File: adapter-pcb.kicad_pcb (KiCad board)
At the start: 2 copper layers, 90.2 x 95.9 mm, 37 parts, among them J1 SS5-80-3.50-L-D-K-TR, J2 DM3BT-DSF-PEJS, J3 Conn_02x05_Odd_Even, U1 TXS0102QDCURQ1, U2 LTC4300A-1IMS8_PBF, U3 TXS02612RTWR

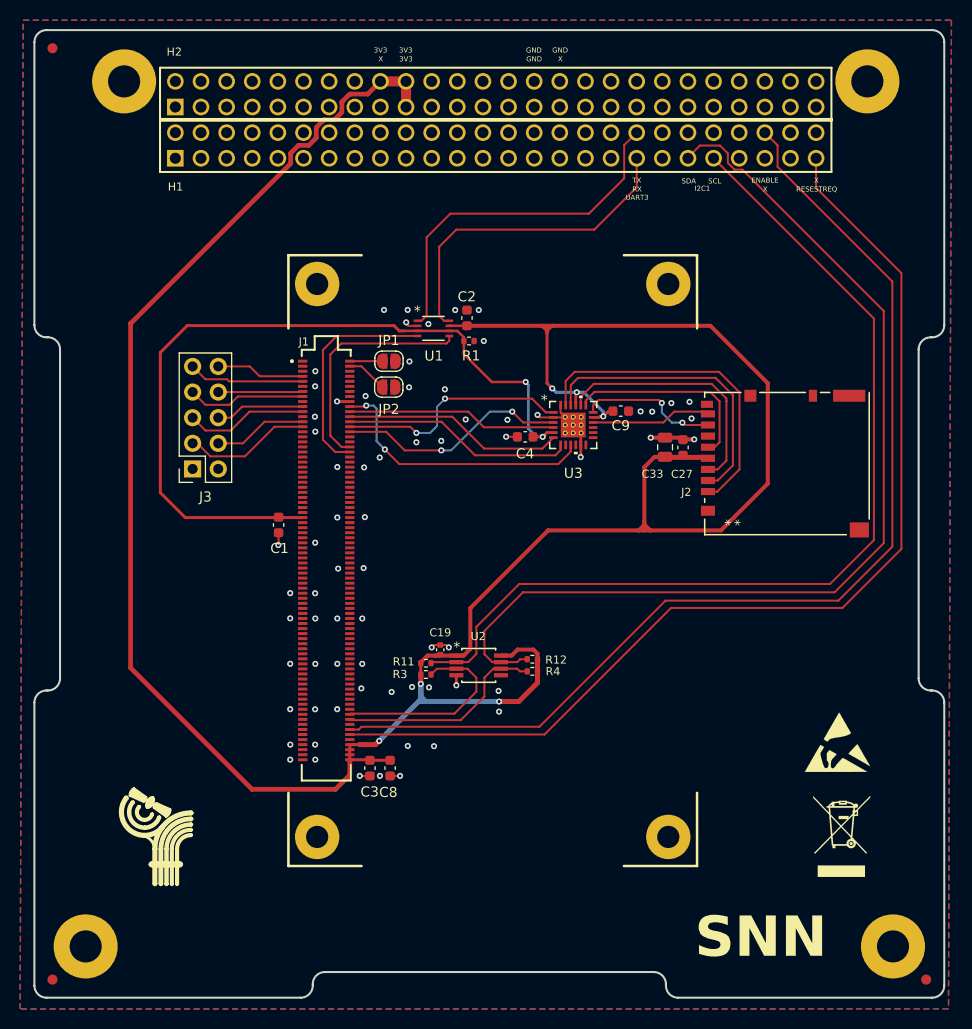
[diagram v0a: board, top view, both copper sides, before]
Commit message: Changed connector orientation and power changes
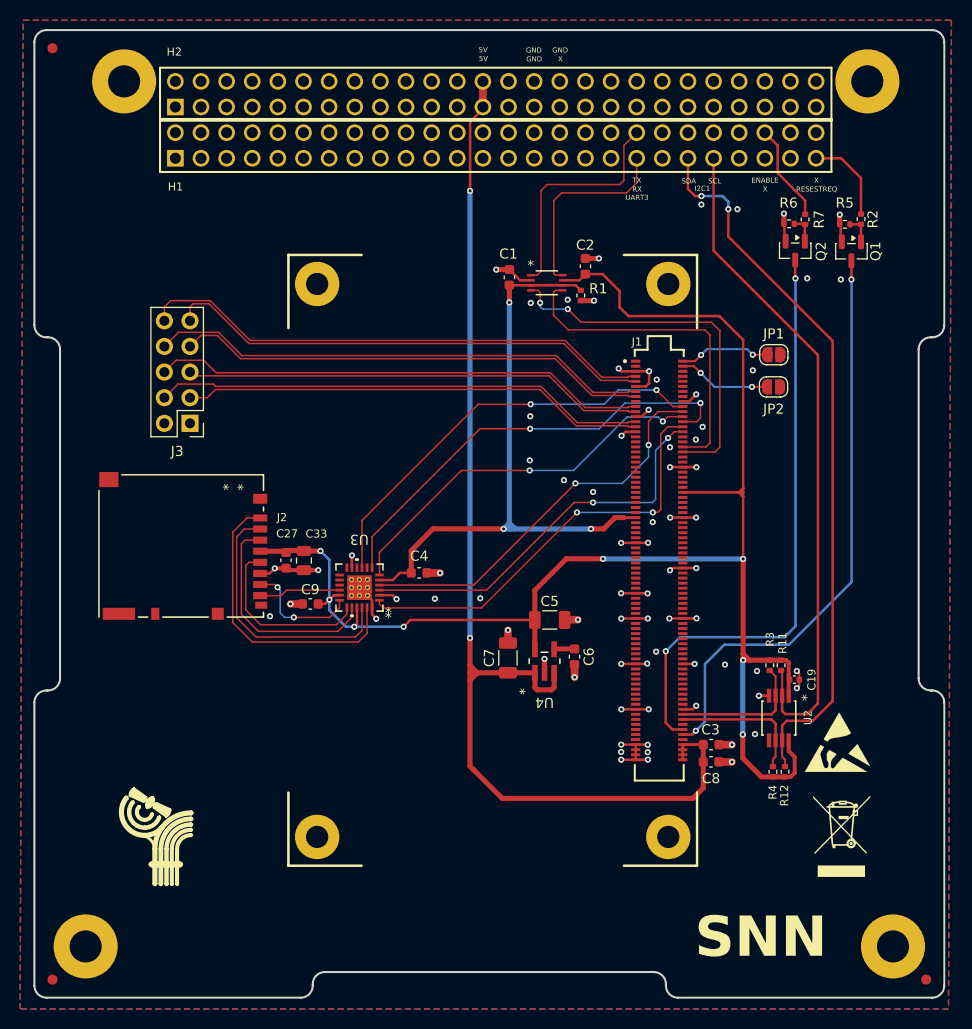
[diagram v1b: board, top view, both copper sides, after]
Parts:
- added C5: 1u, Capacitor_SMD:C_1206_3216Metric, F.Cu at (156.5, 105.0)
- added C6: 0.1u, Capacitor_SMD:C_0603_1608Metric, F.Cu at (158.9, 108.6)
- added C7: 1u, Capacitor_SMD:C_1206_3216Metric, F.Cu at (152.3, 108.7)
- added Q1: 2N7002KQ-7, Package_TO_SOT_SMD:SOT-23, F.Cu at (186.4, 68.4)
- added Q2: 2N7002KQ-7, Package_TO_SOT_SMD:SOT-23, F.Cu at (180.8, 68.4)
- added R2: 100, Resistor_SMD:R_0402_1005Metric, F.Cu at (187.3, 65.2)
- added R5: 100K, Resistor_SMD:R_0402_1005Metric, F.Cu at (185.7, 65.7)
- added R6: 100K, Resistor_SMD:R_0402_1005Metric, F.Cu at (180.2, 65.7)
- added R7: 100, Resistor_SMD:R_0402_1005Metric, F.Cu at (181.8, 65.3)
- added U4: TPS79933QDDCRQ1, adapter:DDC5, F.Cu at (156.0, 109.0)
- J3: moved to B.Cu
- moved MH5 64.9 mm to (168.2, 126.5), turned to 180 degrees
- moved MH6 64.9 mm to (133.4, 126.5), turned to 180 degrees
- moved MH7 64.9 mm to (168.2, 71.7), turned to 180 degrees
- moved MH8 64.9 mm to (133.4, 71.7), turned to 180 degrees
- moved J2 60.6 mm to (120.0, 97.6), turned to -90 degrees
- moved C27 40.9 mm to (130.3, 99.0), turned to -90 degrees
- moved JP1 38.1 mm to (178.7, 78.7)
- moved JP2 38.1 mm to (178.7, 81.9)
- moved C33 37.5 mm to (132.1, 99.1), turned to -90 degrees
- moved C9 36.2 mm to (132.8, 103.4), turned to 0 degrees
- moved C19 35.2 mm to (180.7, 110.9), turned to 180 degrees
- moved R11 35.2 mm to (179.4, 109.5), turned to -90 degrees
- moved R3 34.1 mm to (178.3, 109.5), turned to -90 degrees
- moved C3 33.9 mm to (172.5, 117.3), turned to 0 degrees
- moved C1 33.5 mm to (152.5, 71.0), turned to -90 degrees
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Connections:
- C3 pad 1: +3V3 -> +5V
- C8 pad 2: +3V3 -> +5V
- H1 pad 51: /CSKB/RESETREQ -> /CSKB/RESET
- H2 pad 18: +3V3 -> unconnected-(H2-Pin_18-Pad18)
- H2 pad 19: +3V3 -> unconnected-(H2-Pin_19-Pad19)
- H2 pad 20: +3V3 -> unconnected-(H2-Pin_20-Pad20)
- H2 pad 25: unconnected-(H2-Pin_25-Pad25) -> +5V
- H2 pad 26: unconnected-(H2-Pin_26-Pad26) -> +5V
- J1 pad 101: (no net) -> unconnected-(J1A-PF3_P-Pad101)
- J1 pad 148: /CSKB/ENABLE -> /TE0724 Connector/ONKEY
- J1 pad 150: /CSKB/RESETREQ -> /TE0724 Connector/RESETREQ
- J1 pad 154: +3V3 -> +5V
- J1 pad 156: +3V3 -> +5V
- J1 pad 158: +3V3 -> +5V
- J1 pad 160: +3V3 -> +5V
- J1 pad 34: unconnected-(J1A-SD-CD_R-Pad34) -> GND
- J1 pad 54: unconnected-(J1A-VCCIO35-Pad54) -> +3V3
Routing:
- net +5V: track 0.00 -> 114.7 mm, vias 0 -> 2
- net +3V3: track 264.4 -> 154.8 mm, vias 6 -> 8
- net /CSKB/RESETREQ: track 104.5 -> 0.00 mm
- net /CSKB/ENABLE: track 107.6 -> 9.74 mm
- net /TE0724 Connector/ONKEY: track 0.00 -> 59.3 mm, vias 0 -> 2
- net GND: track 22.1 -> 80.4 mm, vias 70 -> 75
- net /TE0724 Connector/RESETREQ: track 0.00 -> 58.2 mm, vias 0 -> 2
- net PHY_MDI0_P: track 8.80 -> 51.5 mm
- net PHY_MDI1_P: track 8.49 -> 49.8 mm
- net PHY_MDI2_P: track 8.82 -> 49.2 mm
- net PHY_MDI3_P: track 9.25 -> 48.9 mm
- net PHY_MDI0_N: track 11.5 -> 48.9 mm
- net PHY_MDI1_N: track 11.8 -> 47.1 mm
- net PHY_MDI2_N: track 12.2 -> 45.8 mm
- net PHY_MDI3_N: track 12.7 -> 46.0 mm
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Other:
- board text added: "5V"
- board text removed: "3V3"

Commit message: reviewed changes to PCB
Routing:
- net /CSKB/UART-TXD LS: track 23.4 -> 19.2 mm
- net /CSKB/UART-RXD LS: track 19.6 -> 15.4 mm
- net /SD Level Shifter/SD-D3: track 39.4 -> 36.6 mm
- net /SD Level Shifter/SD-D2: track 42.5 -> 40.2 mm
- net /SD Level Shifter/SD-CMD: track 39.3 -> 37.2 mm
- net /CSKB/I2C_SDA_CSKB: track 71.6 -> 70.1 mm
- net /TE0724 Connector/ONKEY: track 59.3 -> 57.8 mm
- net /SD Level Shifter/SD-D1: track 44.5 -> 43.5 mm

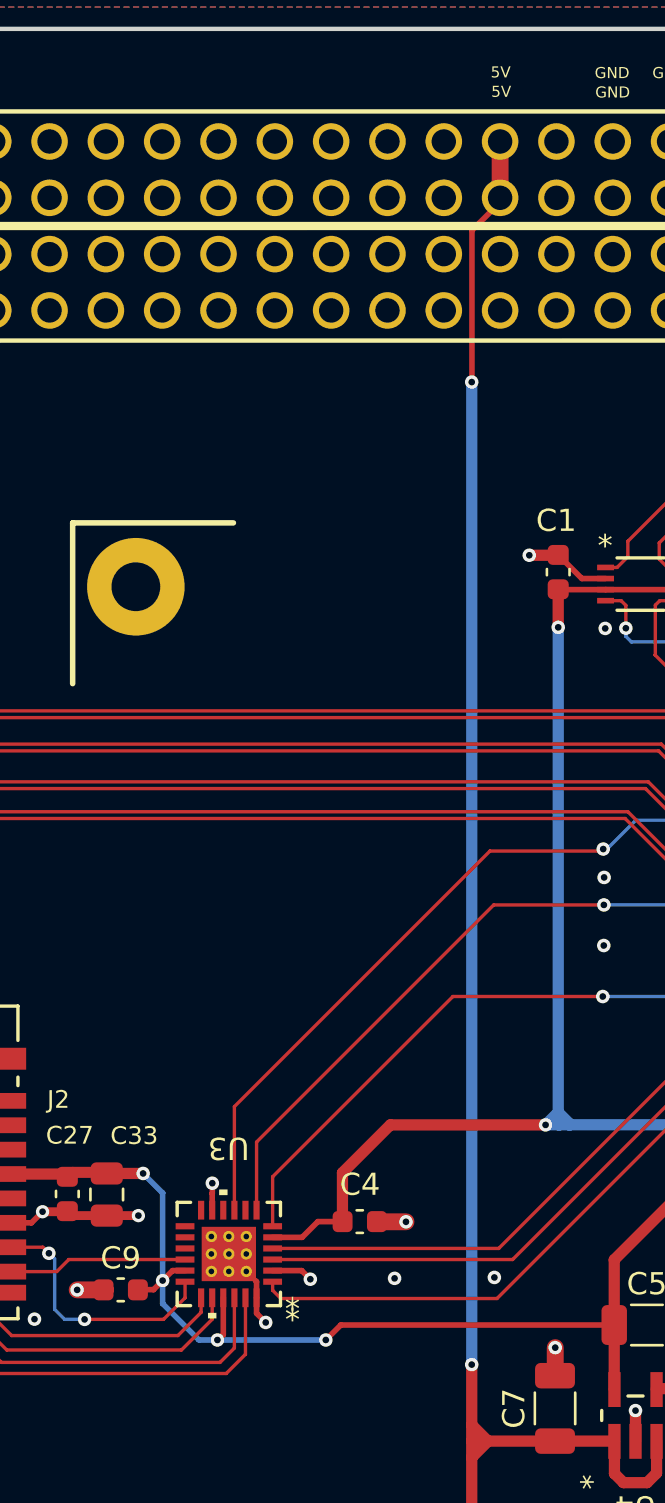
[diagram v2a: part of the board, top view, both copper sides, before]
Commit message: added mroe GND pins and moved power to PDM lines
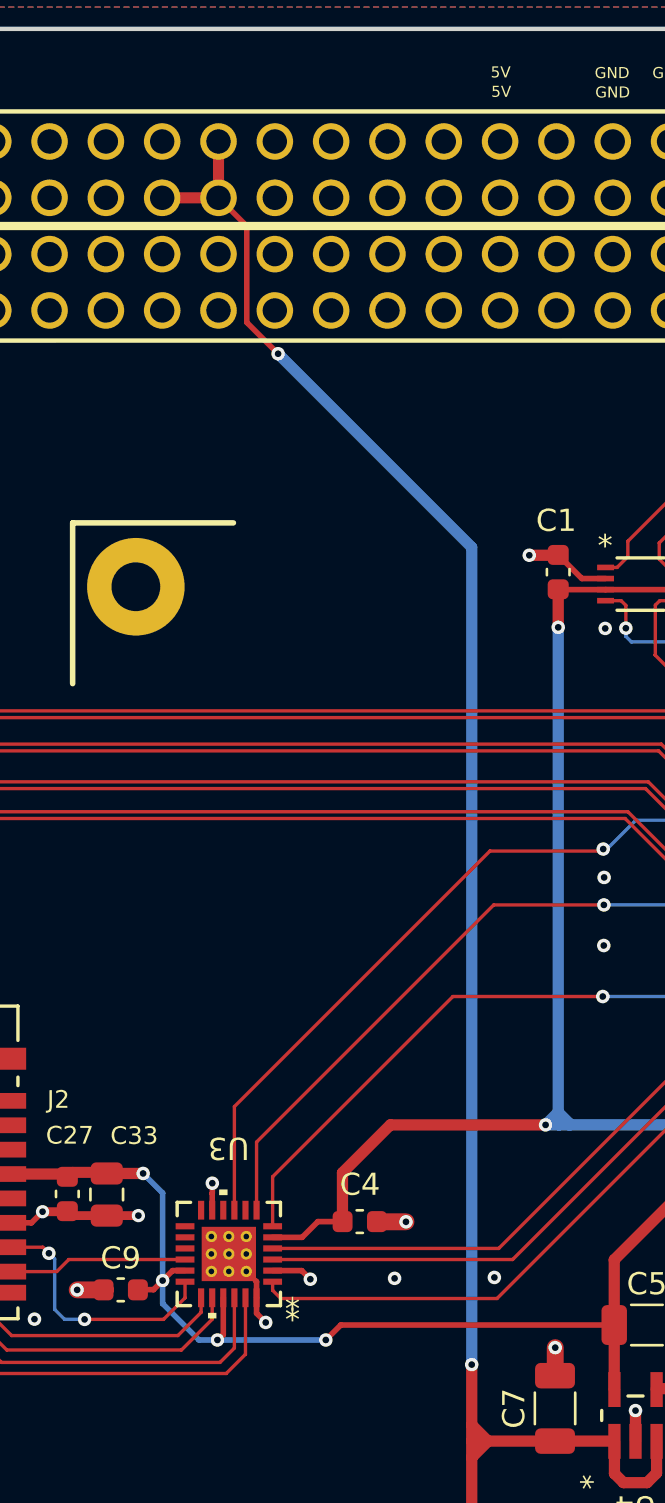
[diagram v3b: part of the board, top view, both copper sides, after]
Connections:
- H2 pad 13: unconnected-(H2-Pin_13-Pad13) -> +5V
- H2 pad 14: unconnected-(H2-Pin_14-Pad14) -> GND
- H2 pad 15: unconnected-(H2-Pin_15-Pad15) -> +5V
- H2 pad 16: unconnected-(H2-Pin_16-Pad16) -> +5V
- H2 pad 17: unconnected-(H2-Pin_17-Pad17) -> GND
- H2 pad 21: unconnected-(H2-Pin_21-Pad21) -> GND
- H2 pad 22: unconnected-(H2-Pin_22-Pad22) -> GND
- H2 pad 25: +5V -> unconnected-(H2-Pin_25-Pad25)
- H2 pad 26: +5V -> unconnected-(H2-Pin_26-Pad26)
- H2 pad 47: unconnected-(H2-Pin_47-Pad47) -> GND
- H2 pad 48: unconnected-(H2-Pin_48-Pad48) -> GND
- H2 pad 9: unconnected-(H2-Pin_9-Pad9) -> GND
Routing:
- net +5V: track 114.8 -> 121.6 mm

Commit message: Made very tiny tweaks
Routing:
- net /TE0724 Connector/ONKEY: track 57.8 -> 55.9 mm
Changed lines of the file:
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@@
 		(tags "TXS02612RTWR ")
 		(property "Reference" "U3"
-			(at 0.010315 4.775 180)
+			(at 1.890661 3.561222 0)
 			(unlocked yes)
 			(layer "F.SilkS")
 			(effects
 				(font
-					(size 1 1)
+					(size 0.8 0.8)
 					(thickness 0.15)
 				)
@@
 			(layer "F.SilkS")
 		)
+		(fp_circle
+			(center -3.25 -3.05)
+			(end -3.25 -3)
+			(stroke
+				(width 0.4)
+				(type solid)
+			)
+			(fill no)
+			(layer "F.SilkS")
+		)
 		(fp_poly
 			(pts
@@
 			(layer "F.Fab")
 		)
-		(fp_text user "*"
-			(at -2.869685 -2.485 0)
-			(layer "F.SilkS")
-			(effects
-				(font
-					(size 1 1)
-					(thickness 0.15)
-				)
-			)
-		)
-		(fp_text user "*"
-			(at -2.869685 -2.485 180)
-			(unlocked yes)
-			(layer "F.SilkS")
-			(effects
-				(font
-					(size 1 1)
-					(thickness 0.15)
-				)
-			)
-		)
 		(fp_text user "${REFERENCE}"
 			(at 0 0 180)
@@
 			(effects
 				(font
-					(size 1.27 1.27)
+					(size 0.8 0.8)
+					(thickness 0.15)
 				)
 			)
@@
 		(tags "capacitor")
 		(property "Reference" "C4"
-			(at -0.01 1.67 0)
+			(at -0.01 1.326222 0)
 			(layer "F.SilkS")
 			(effects
 				(font
-					(size 1 1)
+					(size 0.8 0.8)
 					(thickness 0.15)
 				)
@@
 			(effects
 				(font
-					(size 1 1)
+					(size 0.8 0.8)
 					(thickness 0.15)
 				)
@@
 			(effects
 				(font
-					(size 1 1)
+					(size 0.8 0.8)
 					(thickness 0.15)
 				)
@@
 			(effects
 				(font
-					(size 1 1)
+					(size 0.8 0.8)
 					(thickness 0.15)
 				)
@@
 			(effects
 				(font
-					(size 1 1)
+					(size 0.8 0.8)
 					(thickness 0.15)
 				)
@@
 			(effects
 				(font
-					(size 1 1)
+					(size 0.8 0.8)
 					(thickness 0.15)
 				)
@@
 			(effects
 				(font
-					(size 1 1)
+					(size 0.8 0.8)
 					(thickness 0.15)
 				)
@@
 		(tags "resistor")
 		(property "Reference" "R1"
-			(at -0.68 -1.73 180)
+			(at 1.84 0 270)
 			(layer "F.SilkS")
 			(effects
 				(font
-					(size 1 1)
+					(size 0.8 0.8)
 					(thickness 0.15)
 				)
@@
 		(tags "capacitor")
 		(property "Reference" "C2"
-			(at -2.105 0.02 0)
+			(at -2.565 0.02 90)
 			(layer "F.SilkS")
 			(effects
 				(font
-					(size 1 1)
+					(size 0.8 0.8)
 					(thickness 0.15)
 				)
@@
 		(tags "capacitor")
 		(property "Reference" "C33"
-			(at -2.65 -1.24 0)
+			(at -3.205 -0.015 90)
 			(layer "F.SilkS")
 			(effects
@@
 			(effects
 				(font
-					(size 1 1)
+					(size 0.8 0.8)
 					(thickness 0.15)
 				)
@@
 		(tags "DM3BT-DSF-PEJS ")
 		(property "Reference" "J2"
-			(at -2.83 -9.98 0)
+			(at -7.981222 -7.474339 0)
 			(unlocked yes)
 			(layer "F.SilkS")
@@
 			(effects
 				(font
-					(size 1 1)
+					(size 0.8 0.8)
 					(thickness 0.15)
 				)
@@
 		(tags "TPS79933QDDCRQ1 ")
 		(property "Reference" "U4"
-			(at -4.111599 0 180)
+			(at -3.156599 -0.005901 0)
 			(unlocked yes)
 			(layer "F.SilkS")
 			(effects
 				(font
-					(size 1 1)
+					(size 0.8 0.8)
 					(thickness 0.15)
 				)
@@
 			(effects
 				(font
-					(size 1 1)
+					(size 0.8 0.8)
 					(thickness 0.15)
 				)
@@
 			(effects
 				(font
-					(size 1 1)
+					(size 0.8 0.8)
 					(thickness 0.15)
 				)
@@
 			(effects
 				(font
-					(size 1 1)
+					(size 0.8 0.8)
 					(thickness 0.15)
 				)
@@
 			(effects
 				(font
-					(size 1 1)
+					(size 0.8 0.8)
 					(thickness 0.15)
 				)
@@
 			(effects
 				(font
-					(size 1 1)
+					(size 0.8 0.8)
 					(thickness 0.15)
 				)
@@
 			(effects
 				(font
-					(size 1 1)
+					(size 0.8 0.8)
 					(thickness 0.15)
 				)
@@
 		(tags "capacitor")
 		(property "Reference" "C19"
-			(at -1.71 -0.005 90)
+			(at -2.43 -0.005 180)
 			(layer "F.SilkS")
 			(effects
@@
 		(tags "capacitor")
 		(property "Reference" "C1"
-			(at -2.32 0.09 0)
+			(at -2.585 -0.005 90)
 			(layer "F.SilkS")
 			(effects
 				(font
-					(size 1 1)
+					(size 0.8 0.8)
 					(thickness 0.15)
 				)
@@
 			(effects
 				(font
-					(size 1 1)
+					(size 0.8 0.8)
 					(thickness 0.15)
 				)
@@
 		(tags "capacitor")
 		(property "Reference" "C27"
-			(at -2.64 -0.11 0)
+			(at -3.105466 -0.01752 90)
 			(layer "F.SilkS")
 			(effects
@@
 			(effects
 				(font
-					(size 1 1)
+					(size 0.8 0.8)
 					(thickness 0.15)
 				)
@@
 		(tags "TXS0102QDCURQ1 ")
 		(property "Reference" "U1"
-			(at 0.0448 2.73 0)
+			(at 0.02 -2.3 0)
 			(unlocked yes)
 			(layer "F.SilkS")
-			(hide yes)
 			(effects
 				(font
-					(size 1 1)
+					(size 0.8 0.8)
 					(thickness 0.15)
 				)
@@
 			(effects
 				(font
-					(size 1 1)
+					(size 0.8 0.8)
 					(thickness 0.15)
 				)
@@
 			(effects
 				(font
-					(size 1 1)
+					(size 0.8 0.8)
 					(thickness 0.15)
 				)
@@
 			(effects
 				(font
-					(size 1 1)
+					(size 0.8 0.8)
 					(thickness 0.15)
 				)
@@
 			(effects
 				(font
-					(size 1 1)
+					(size 0.8 0.8)
 					(thickness 0.15)
 				)
@@
 		(property "Reference" "J3"
 			(at -1.27 2.77 180)
-			(layer "F.SilkS")
+			(layer "B.SilkS")
 			(effects
 				(font
-					(size 1 1)
+					(size 0.8 0.8)
 					(thickness 0.15)
 				)
+				(justify mirror)
 			)
 		)
@@
 				(type solid)
 			)
-			(layer "F.SilkS")
+			(layer "B.SilkS")
 		)
 		(fp_line
@@
 				(type solid)
 			)
-			(layer "F.SilkS")
+			(layer "B.SilkS")
 		)
 		(fp_line
@@
 				(type solid)
 			)
-			(layer "F.SilkS")
+			(layer "B.SilkS")
 		)
 		(fp_line
@@
 				(type solid)
 			)
-			(layer "F.SilkS")
+			(layer "B.SilkS")
 		)
 		(fp_line
@@
 				(type solid)
 			)
-			(layer "F.SilkS")
+			(layer "B.SilkS")
 		)
 		(fp_line
@@
 				(type solid)
 			)
-			(layer "F.SilkS")
+			(layer "B.SilkS")
 		)
 		(fp_line
@@
 				(type solid)
 			)
-			(layer "F.SilkS")
+			(layer "B.SilkS")
 		)
 		(fp_line
@@
 				(type solid)
 			)
-			(layer "F.SilkS")
+			(layer "B.SilkS")
 		)
 		(fp_line
@@
 	)
 	(segment
-		(start 180.83 71.11)
-		(end 180.84 71.12)
+		(start 180.84 99.71)
+		(end 174.285 106.265)
 		(width 0.254)
 		(layer "B.Cu")
@@
 	(segment
 		(start 180.84 71.12)
-		(end 180.84 103.06)
+		(end 180.84 99.71)
 		(width 0.254)
 		(layer "B.Cu")
@@
 	)
 	(segment
-		(start 169.775 106.265)
-		(end 167.98 108.06)
+		(start 174.285 106.265)
+		(end 169.775 106.265)
 		(width 0.254)
 		(layer "B.Cu")
@@
 	)
 	(segment
-		(start 177.635 106.265)
-		(end 169.775 106.265)
+		(start 180.83 71.11)
+		(end 180.84 71.12)
 		(width 0.254)
 		(layer "B.Cu")
@@
 	)
 	(segment
-		(start 180.84 103.06)
-		(end 177.635 106.265)
+		(start 169.775 106.265)
+		(end 167.98 108.06)
 		(width 0.254)
 		(layer "B.Cu")
@@
 	)
 	(segment
+		(start 149.86 54.32)
+		(end 149.86 54.12)
+		(width 0.254)
+		(layer "F.Cu")
+		(net "unconnected-(H2-Pin_25-Pad25)")
+	)
+	(segment
 		(start 152.4 56.66)
 		(end 151.69 56.66)
@@
 		(net "unconnected-(H1-Pin_30-Pad30)")
 	)
-	(segment
-		(start 149.86 54.32)
-		(end 149.86 54.12)
-		(width 0.254)
-		(layer "F.Cu")
-		(net "unconnected-(H2-Pin_25-Pad25)")
-	)
 	(zone
